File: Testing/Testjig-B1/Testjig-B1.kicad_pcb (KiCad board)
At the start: 2 copper layers, 184.9 x 107.9 mm, 77 parts, among them J1 Conn_Coaxial, J2 Conn_Coaxial, U1 LM7805_TO220, U2 LM7815_TO220, U3 LM317_TO-220, U4 LM7915_TO220, U5 LM7924_TO220, U6 74HC14, U7 74HC14, U8 74HC14, U9 74HC14, X1 Conn_02x16_Odd_Even, X2 Conn_02x16_Odd_Even

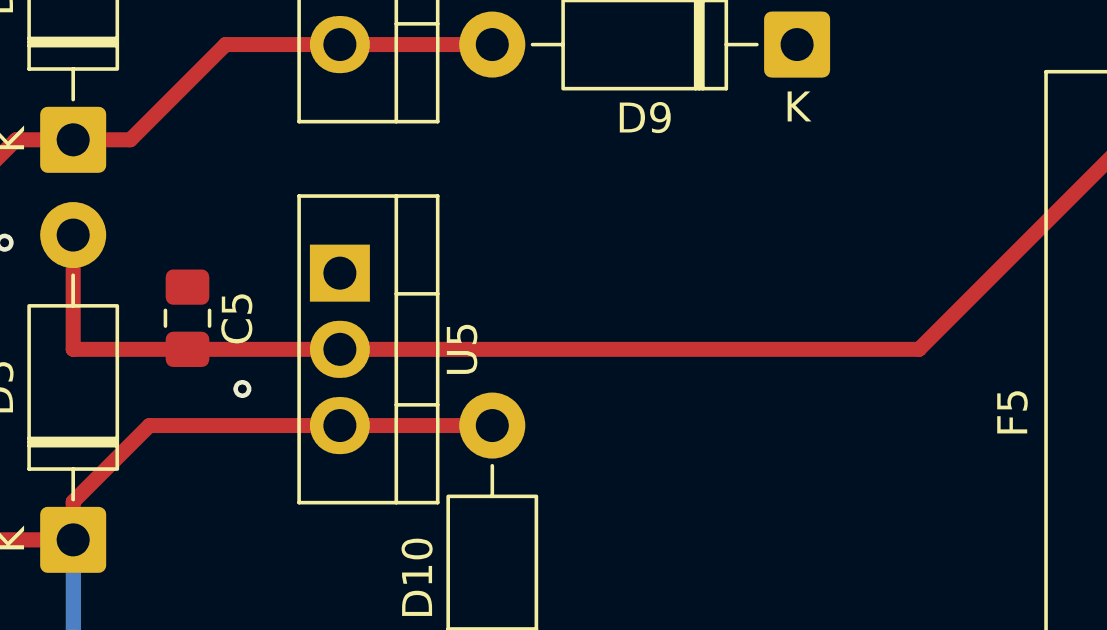
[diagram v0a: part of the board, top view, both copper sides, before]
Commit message: Make +24V actually +20V as the UPL does
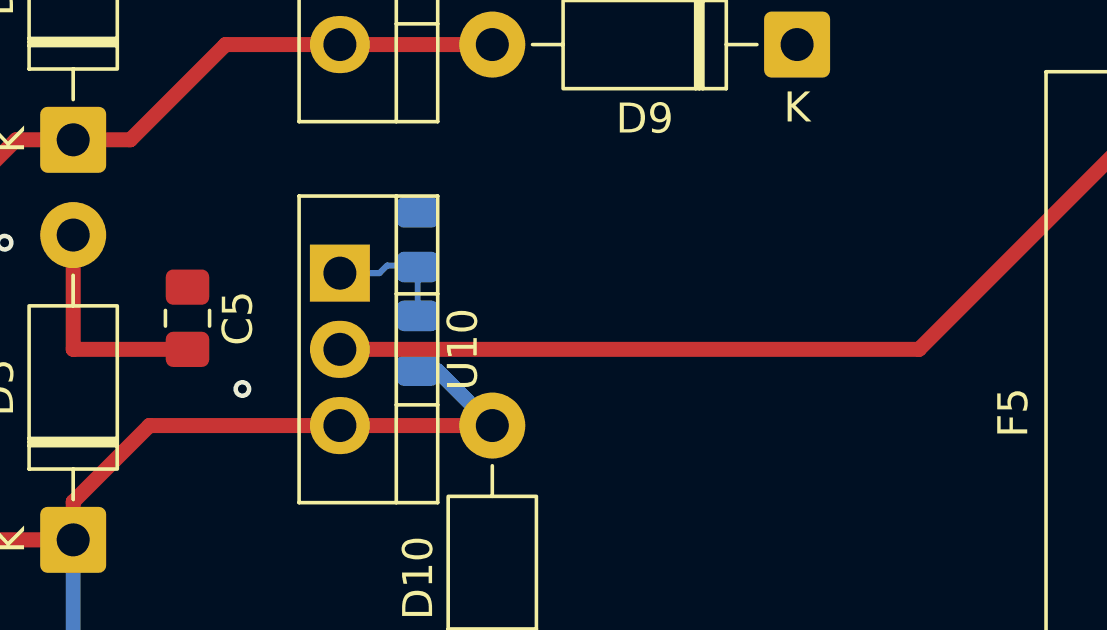
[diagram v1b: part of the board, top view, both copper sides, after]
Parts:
- removed U5: LM7924_TO220, Package_TO_SOT_THT:TO-220-3_Vertical
- added R10: 260R, Resistor_SMD:R_0805_2012Metric, B.Cu at (216.0, 105.2)
- added R17: 1k8, Resistor_SMD:R_0805_2012Metric, B.Cu at (216.0, 101.8)
- added U10: LM337_TO220, Package_TO_SOT_THT:TO-220-3_Vertical, F.Cu at (213.4, 102.9)
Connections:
- X1 pad 1: /LDFREQ_1 -> GND
- X1 pad 10: //IN_WR_1 -> //IN_RD_1
- X1 pad 11: /IN_CLK_1 -> /SDI_1
- X1 pad 12: /SDI_1 -> /IN_CLK_1
- X1 pad 13: +5V -> GND
- X1 pad 14: GND -> +5V
- X1 pad 2: GND -> /LDFREQ_1
- X1 pad 31: /LOW_DIST_1 -> GND
- X1 pad 32: GND -> /LOW_DIST_1
- X1 pad 7: /SDO_1 -> /ENABLE_1
- X1 pad 8: /ENABLE_1 -> /SDO_1
- X1 pad 9: //IN_RD_1 -> //IN_WR_1
- X2 pad 1: /LDFREQ_2 -> GND
- X2 pad 10: //IN_WR_2 -> //IN_RD_2
- X2 pad 11: /IN_CLK_2 -> /SDI_2
- X2 pad 12: /SDI_2 -> /IN_CLK_2
- X2 pad 13: +5V -> GND
- X2 pad 14: GND -> +5V
- X2 pad 2: GND -> /LDFREQ_2
- X2 pad 31: /LOW_DIST_2 -> GND
- X2 pad 32: GND -> /LOW_DIST_2
- X2 pad 7: /SDO_2 -> /ENABLE_2
- X2 pad 8: /ENABLE_2 -> /SDO_2
- X2 pad 9: //IN_RD_2 -> //IN_WR_2
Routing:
- net Net-(D5-A): track 44.9 -> 39.9 mm
- net Net-(U10-ADJ): track 0.00 -> 4.52 mm
- net -24V: track 94.6 -> 97.8 mm

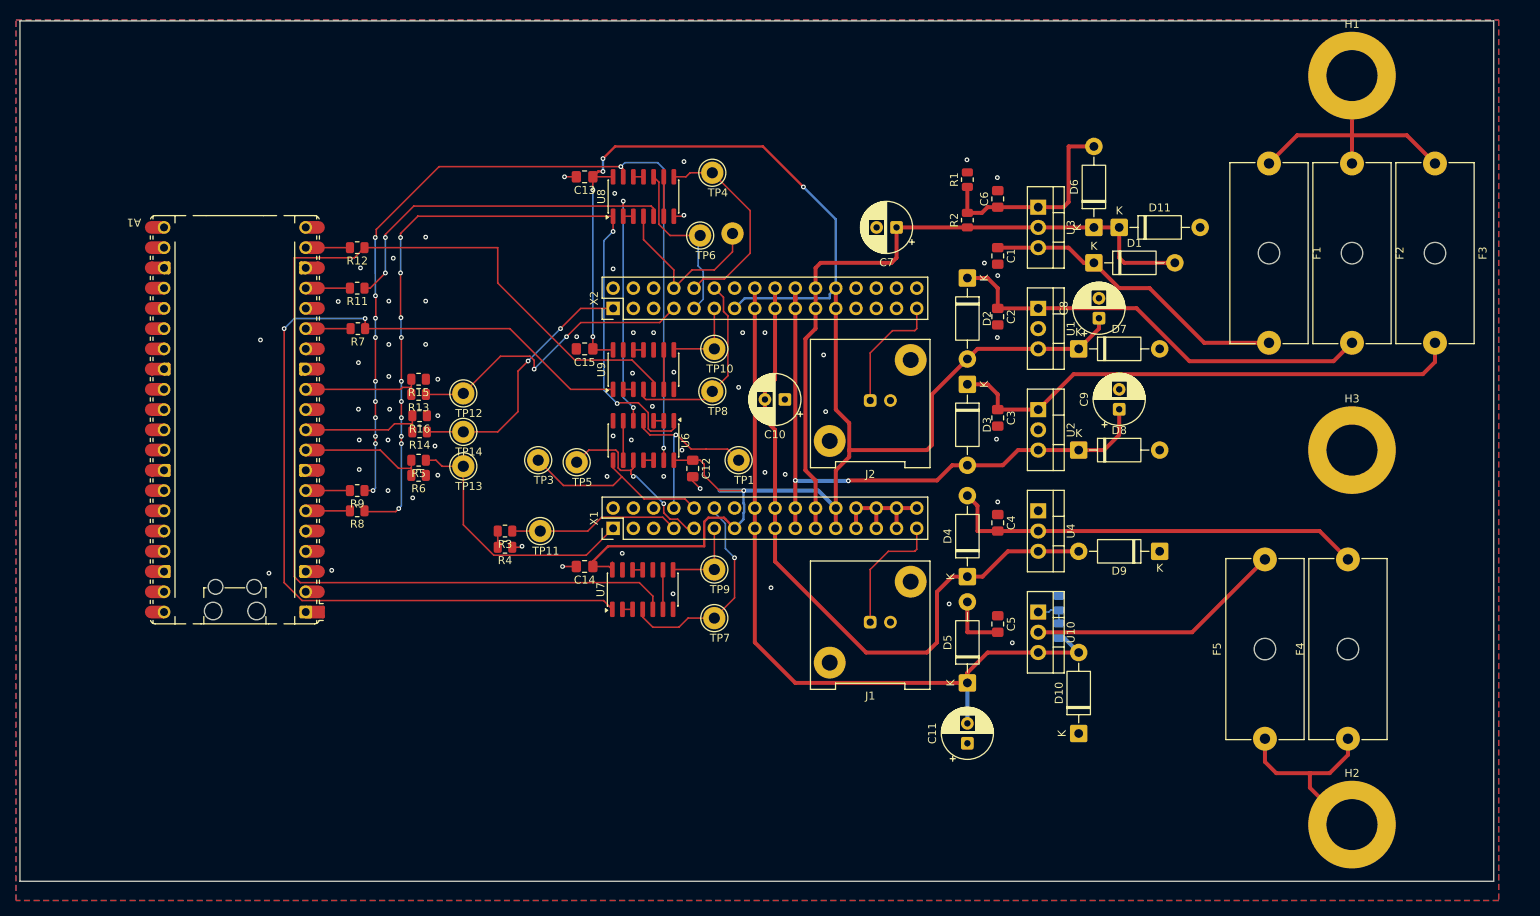
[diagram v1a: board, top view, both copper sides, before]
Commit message: Calculate power requirements and heat sinks.
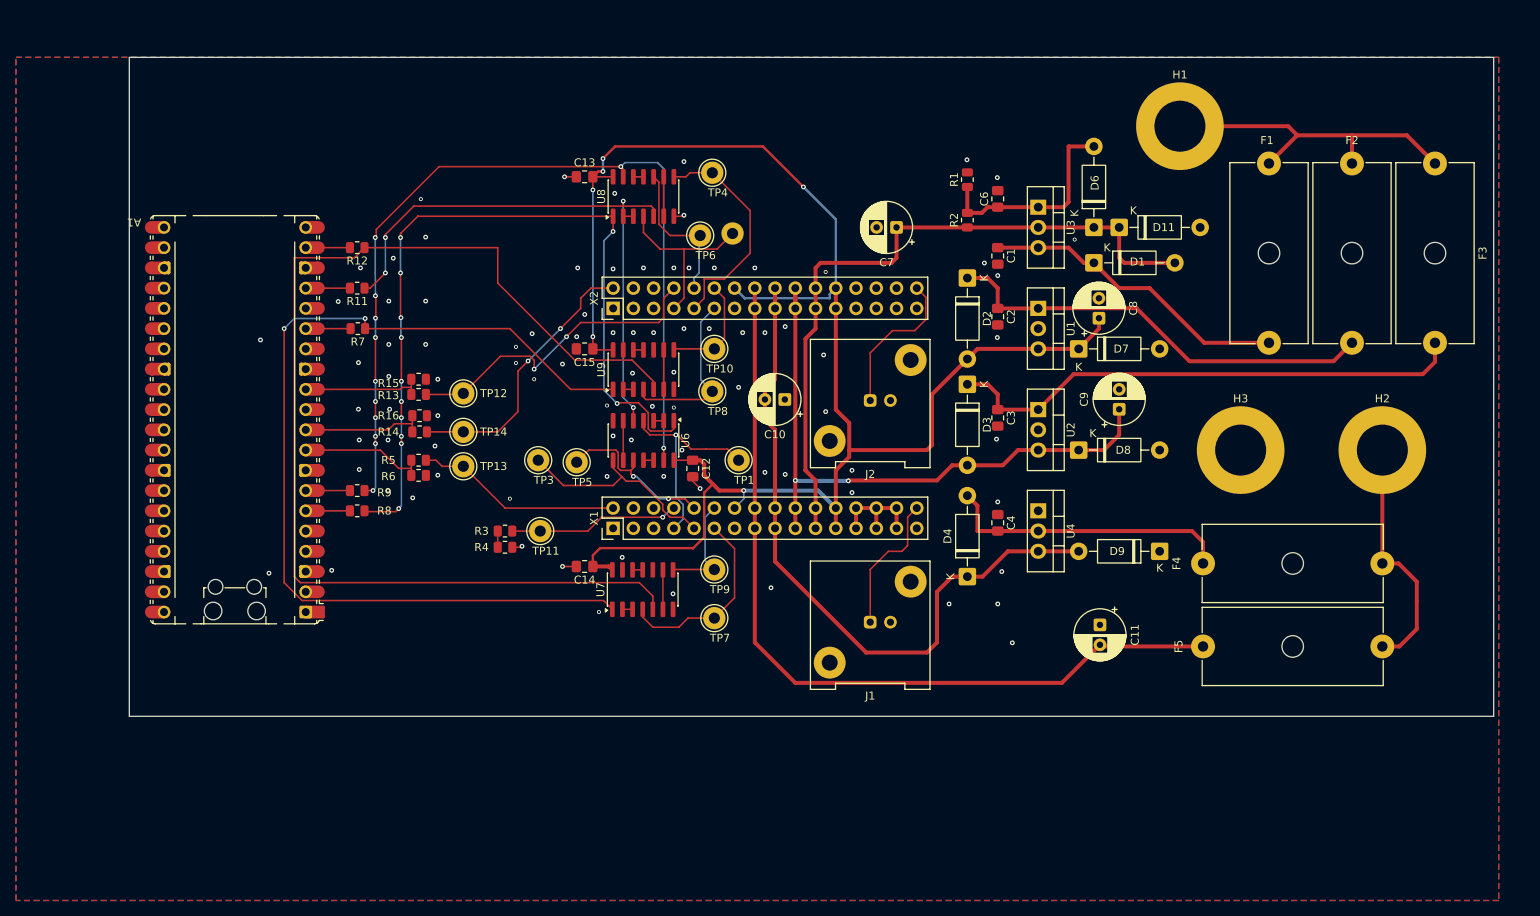
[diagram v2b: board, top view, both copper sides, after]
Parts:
- removed C5: 100nF, Capacitor_SMD:C_0805_2012Metric_Pad1.18x1.45mm_HandSolder
- removed D10, D5: 1N4001, Diode_THT:D_DO-41_SOD81_P10.16mm_Horizontal
- removed R10: 260R, Resistor_SMD:R_0805_2012Metric
- removed R17: 1k8, Resistor_SMD:R_0805_2012Metric
- removed U10: LM337_TO220, Package_TO_SOT_THT:TO-220-3_Vertical
- moved H2 47.1 mm to (256.5, 82.5)
- moved H1 22.5 mm to (231.1, 41.9)
- moved F4 22.4 mm to (256.5, 96.8), turned to 180 degrees
- moved C11 22.3 mm to (221.1, 104.5), turned to -90 degrees
- moved F5 18.7 mm to (256.5, 107.2), turned to 180 degrees
- moved H3 14.0 mm to (238.8, 82.5)
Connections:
- F5 pad 2: Net-(D5-A) -> -24V
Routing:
- net Net-(D5-A): track 39.9 -> 0.00 mm
- net Net-(D4-A): track 52.9 -> 36.5 mm
- net /LDFREQ_1: track 34.1 -> 26.0 mm
- net +VDC: track 34.8 -> 42.5 mm
- net -24V: track 97.8 -> 104.9 mm
- net +5V: track 220.3 -> 214.0 mm
- net -VDC: track 25.9 -> 31.2 mm
- net Net-(U10-ADJ): track 4.52 -> 0.00 mm
- net /IN_CLK_2: track 10.2 -> 13.8 mm
- net /LOW_DIST_2: track 15.6 -> 19.1 mm
- net /IN_CLK_1: track 10.4 -> 13.9 mm
- net /ENABLE_1: track 23.8 -> 27.1 mm
- net //IN_RD_2: track 22.0 -> 18.9 mm
- net /SDI_2: track 24.6 -> 21.9 mm
- net /SDI_1: track 26.9 -> 24.3 mm, vias 1 -> 0
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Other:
- board size 184.9 x 107.9 mm -> 171.2 x 82.7 mm

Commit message: Make board production ready.
- Fix all DRC errors (accept if need)
- Fix all ERC errors (accept if needed)
- Use correct 34 (!) pin connector on board
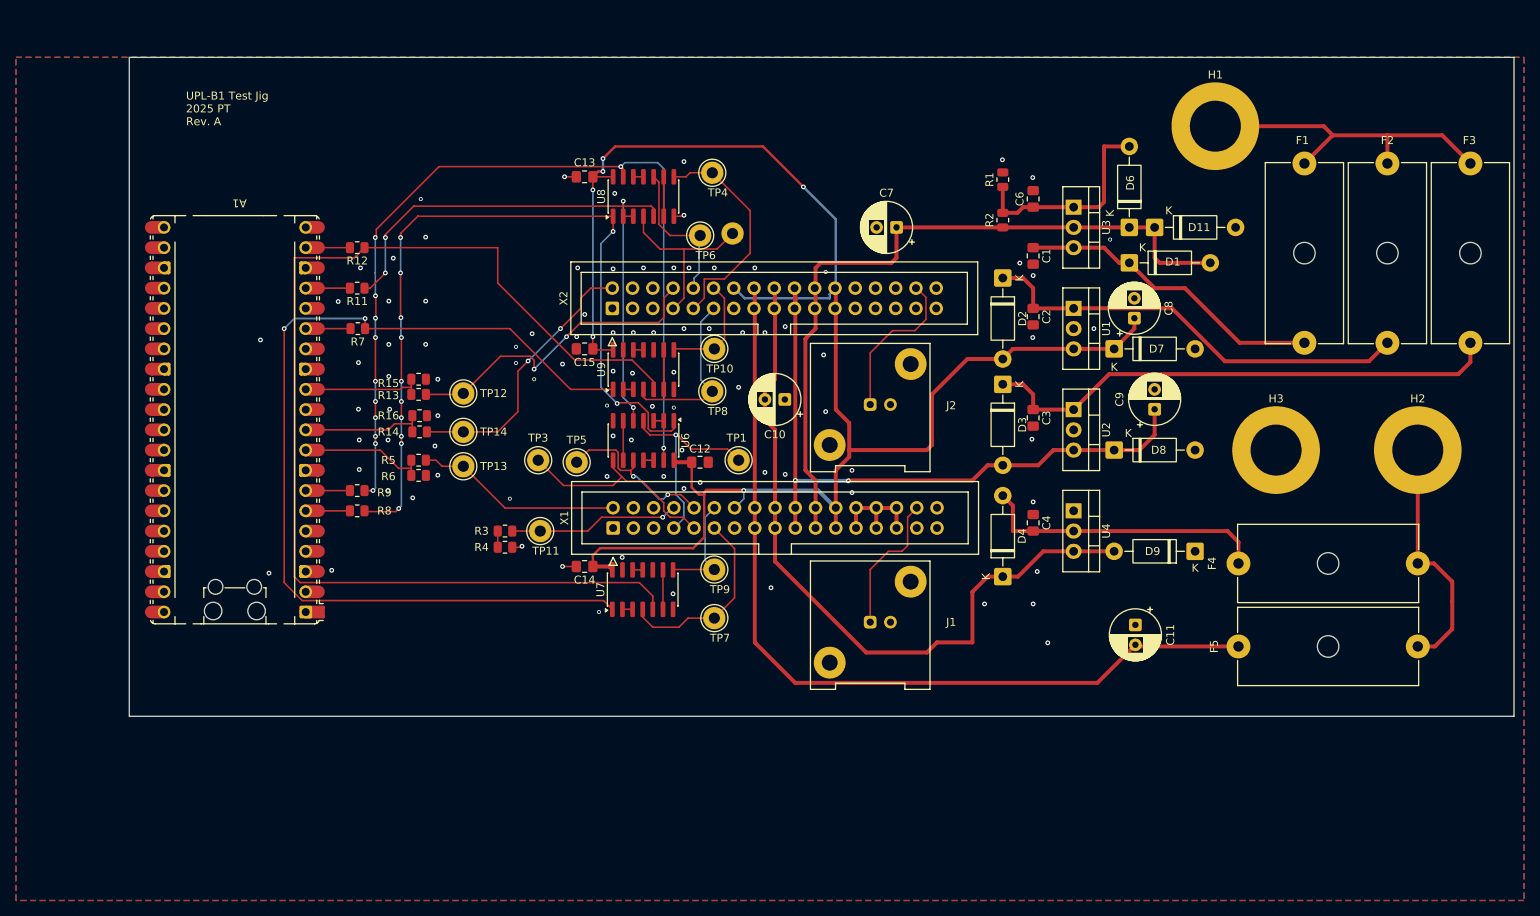
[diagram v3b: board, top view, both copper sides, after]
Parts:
- X1, X2: value Conn_02x16_Odd_Even -> Conn_02x17_Odd_Even; footprint Connector_PinHeader_2.54mm:PinHeader_2x16_P2.54mm_Vertical -> Connector_IDC:IDC-Header_2x17_P2.54mm_Vertical
- moved C8 4.45 mm to (225.4, 66.0)
- moved F2 4.45 mm to (257.2, 46.6)
- moved H1 4.45 mm to (235.6, 41.9)
- moved H3 4.45 mm to (243.2, 82.5)
- moved C1 4.44 mm to (212.7, 58.2)
- moved C11 4.44 mm to (225.6, 104.5)
- moved C2 4.44 mm to (212.7, 65.8)
- moved C3 4.44 mm to (212.7, 78.5)
- moved C4 4.44 mm to (212.7, 91.7)
- moved C6 4.44 mm to (212.7, 51.0)
- moved C9 4.44 mm to (228.0, 77.4)
- moved D1 4.44 mm to (224.8, 59.1)
- moved D11 4.44 mm to (228.0, 54.6)
- moved D2 4.44 mm to (208.9, 61.0)
- moved D3 4.44 mm to (208.9, 74.3)
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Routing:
- net -24V: track 104.9 -> 109.3 mm
- net +15V: track 78.9 -> 83.4 mm
- net +6V: track 87.2 -> 91.7 mm
- net -15V: track 87.2 -> 91.6 mm
- net +5V: track 214.0 -> 218.3 mm
- net GND: track 20.4 -> 18.5 mm, vias 89 -> 92
- net /LOW_DIST_2: track 19.1 -> 19.6 mm
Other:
- board size 171.2 x 82.7 mm -> 173.7 x 82.7 mm
- board text added: "UPL-B1 Test Jig 2025 PT Rev. A"

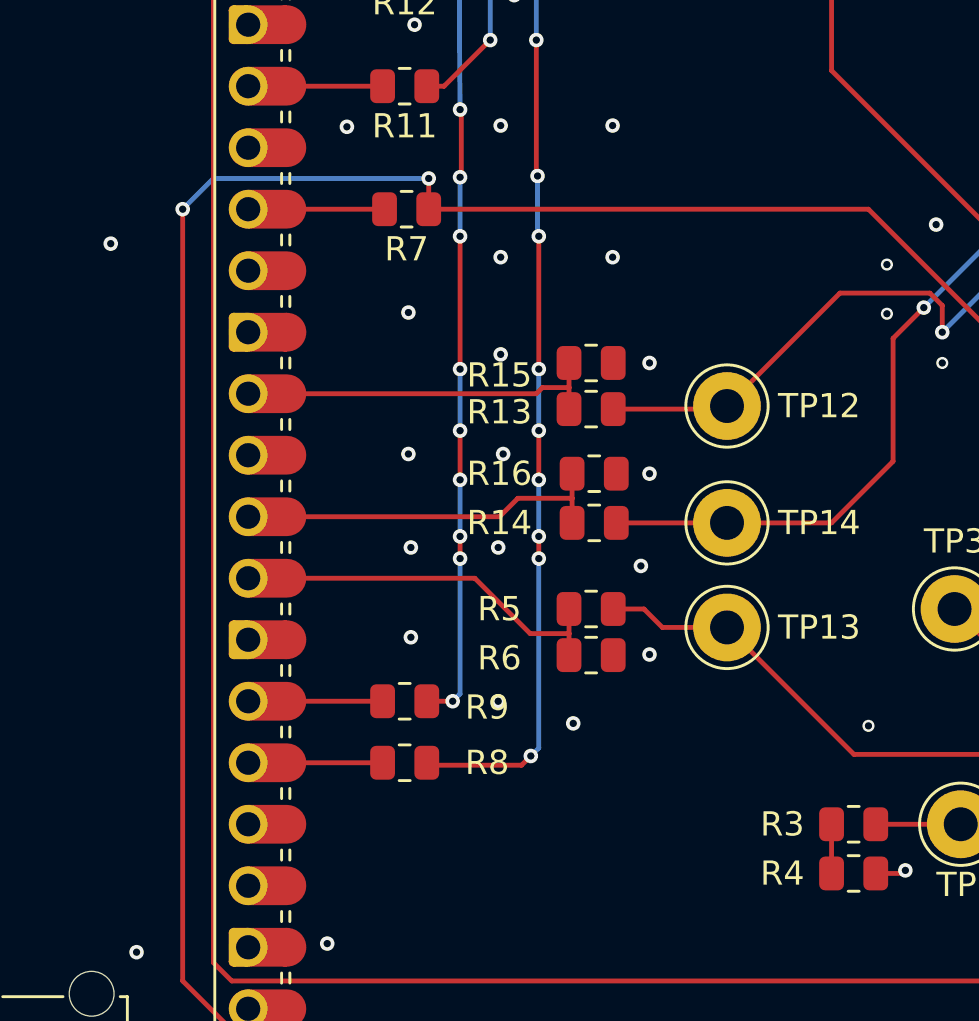
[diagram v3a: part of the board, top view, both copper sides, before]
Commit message: Last fixes before production of Rev A.
- Add signal line for SDO1 which had a break in the schematic.
- Route out said signal
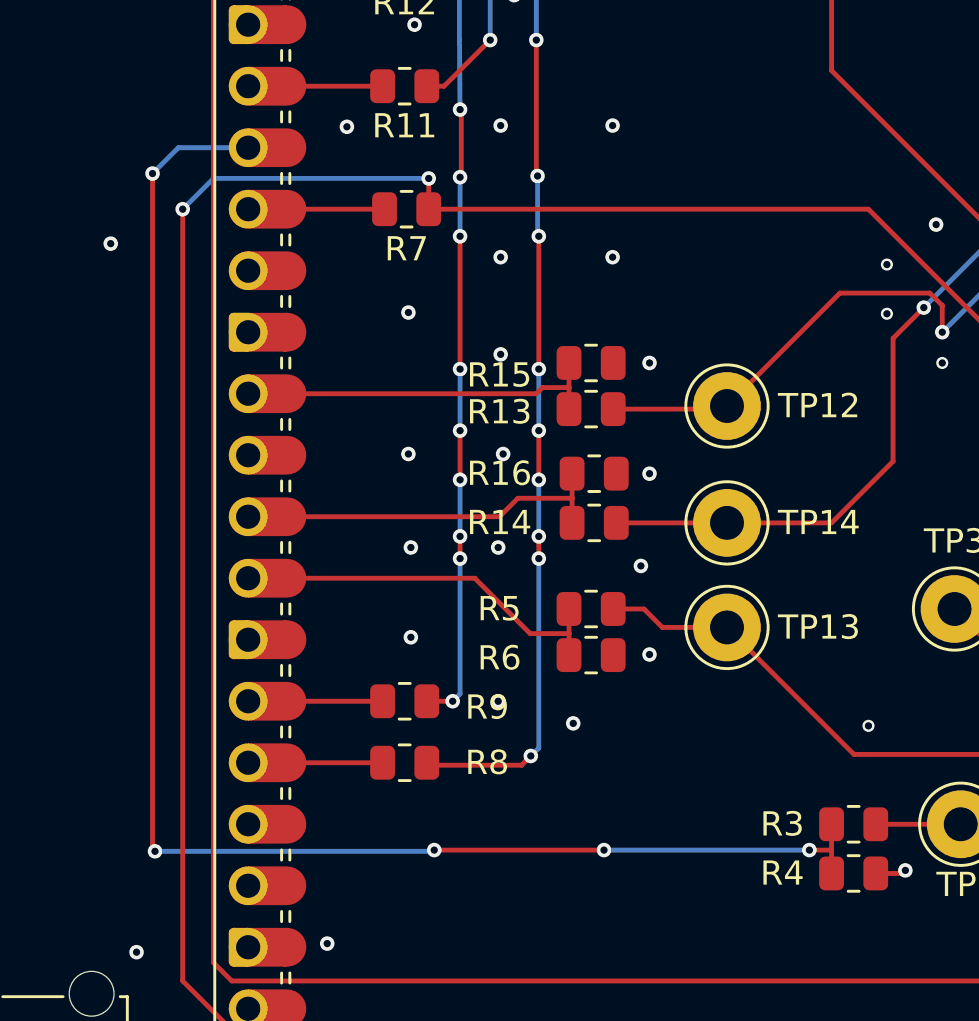
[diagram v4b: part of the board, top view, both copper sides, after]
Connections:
- A1 pad 16: unconnected-(A1-GPIO12-Pad16) -> /CPU/SDO_1_3V3
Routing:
- net /CPU/SDO_1_3V3: track 2.03 -> 62.5 mm, vias 0 -> 5
